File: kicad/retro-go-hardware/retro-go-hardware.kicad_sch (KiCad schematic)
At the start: 1 part

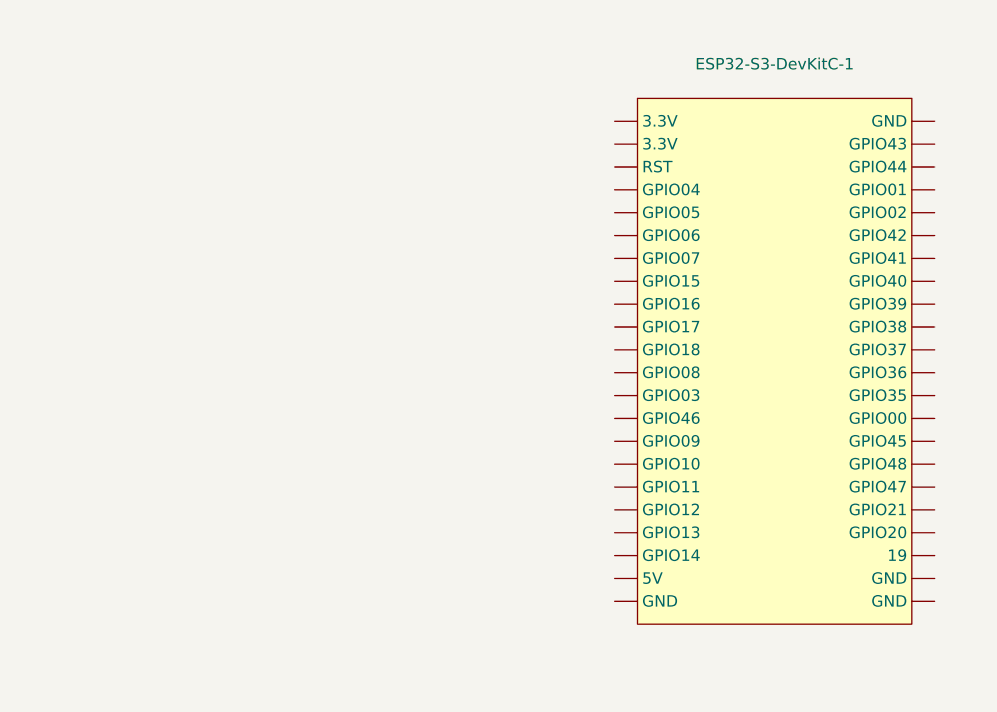
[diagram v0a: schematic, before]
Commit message: Created screen symbol
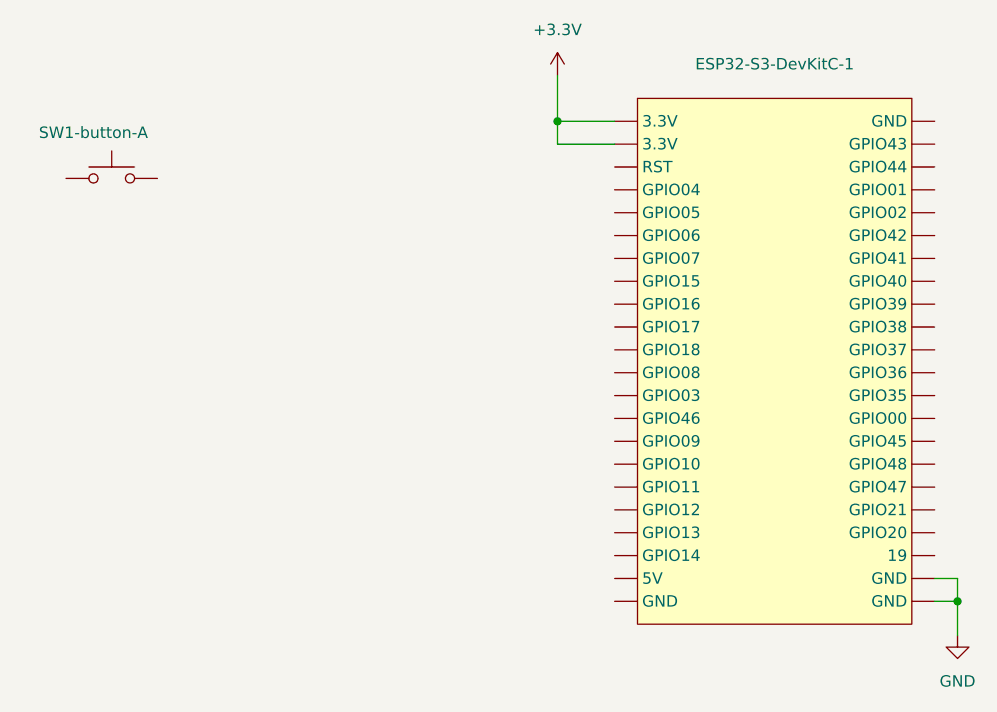
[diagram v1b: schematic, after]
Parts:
- added SW1-button-A: ~, symbol Switch:SW_Push
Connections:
- net GND: now reaches ESP32-S3-DevKitC-1. (RST)
- new net +3.3V: ESP32-S3-DevKitC-1. (RST)

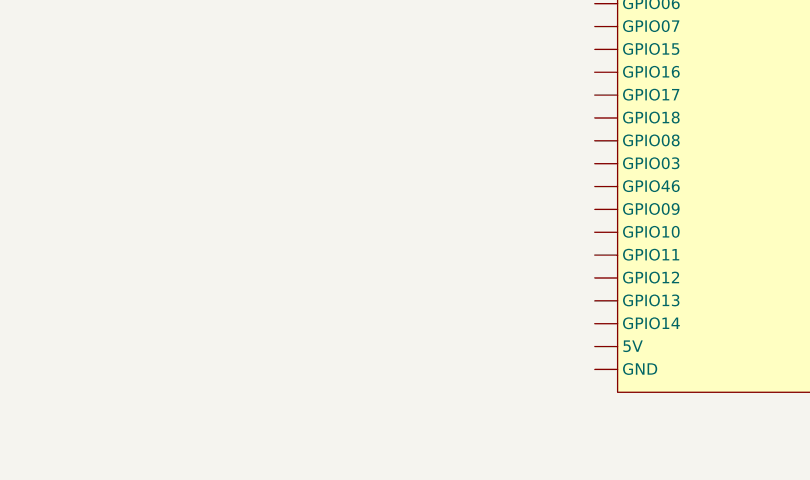
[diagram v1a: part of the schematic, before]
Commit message: Schematics connected SDSPI
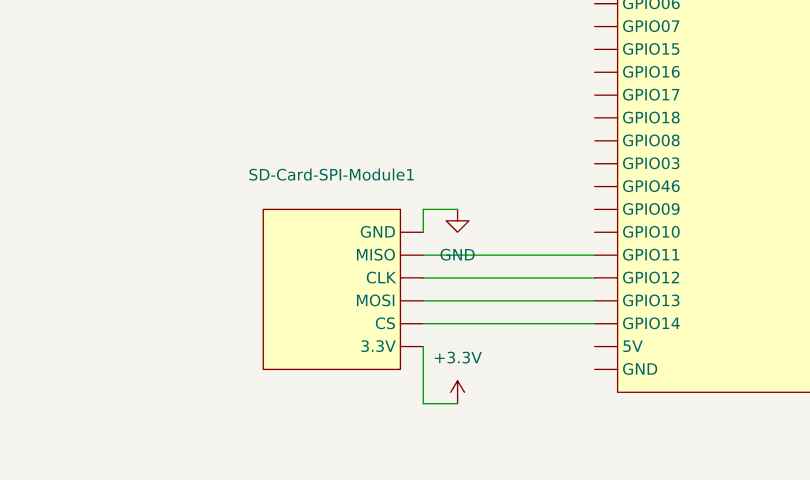
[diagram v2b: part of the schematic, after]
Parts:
- added SD-Card-SPI-Module1: ~, symbol CustomLibrary:SD-Card-SPI-Module
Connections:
- net +3.3V: now also SD-Card-SPI-Module1. (MOSI)
- net GND: now also SD-Card-SPI-Module1. (MOSI)
- new net: ESP32-S3-DevKitC-1. (RST), SD-Card-SPI-Module1. (MOSI) (x4)

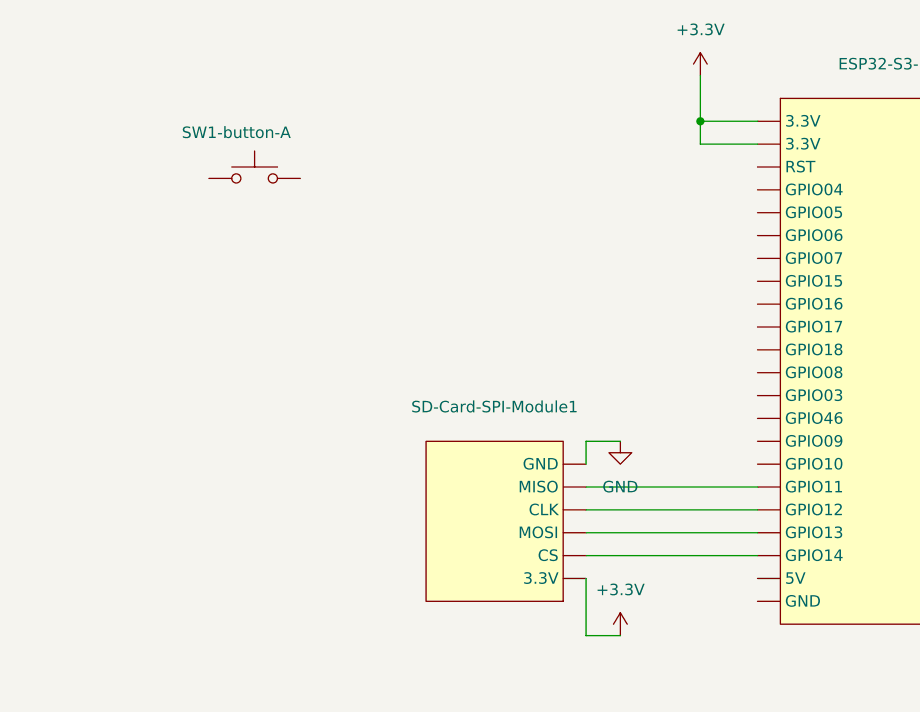
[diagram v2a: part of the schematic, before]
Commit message: Added I2S module to schematic
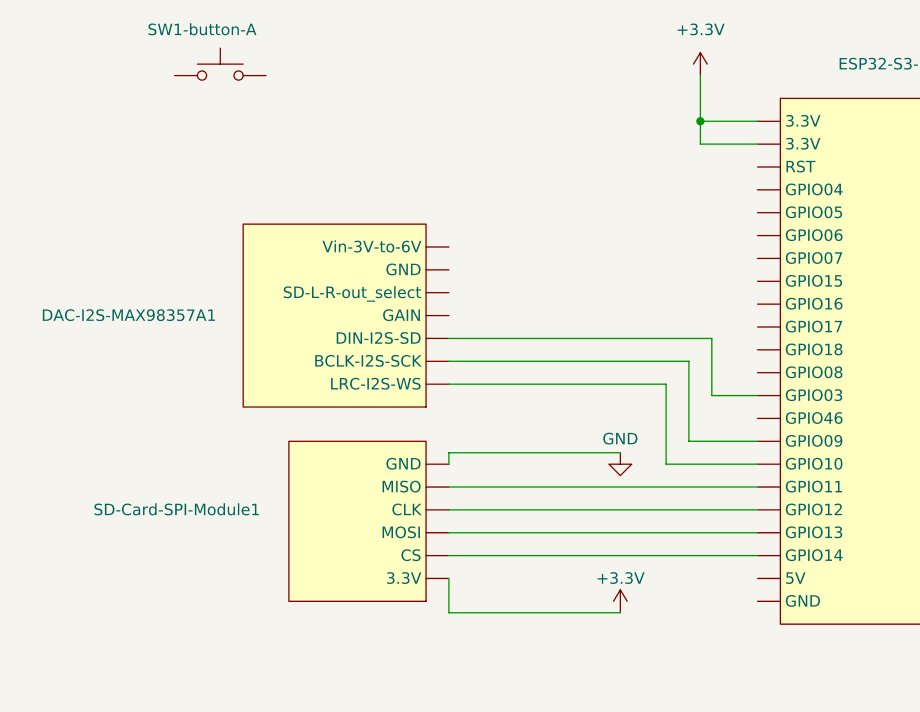
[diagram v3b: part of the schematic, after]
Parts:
- added DAC-I2S-MAX98357A1: ~, symbol CustomLibrary:DAC-I2S-MAX98357A
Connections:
- new net: ESP32-S3-DevKitC-1. (RST), SD-Card-SPI-Module1. (MOSI) (x4)
- new net: DAC-I2S-MAX98357A1. (Vin-3V-to-6V), ESP32-S3-DevKitC-1. (RST) (x3)
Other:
- moved on the sheet: SD-Card-SPI-Module1, SW1-button-A
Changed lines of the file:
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@@
 	(wire
 		(pts
-			(xy 123.19 81.28) (xy 123.19 83.82)
-		)
-		(stroke
-			(width 0)
-			(type default)
-		)
-	)
-	(wire
-		(pts
-			(xy 123.19 96.52) (xy 123.19 102.87)
+			(xy 134.62 72.39) (xy 107.95 72.39)
+		)
+		(stroke
+			(width 0)
+			(type default)
+		)
+	)
+	(wire
+		(pts
+			(xy 107.95 82.55) (xy 107.95 83.82)
+		)
+		(stroke
+			(width 0)
+			(type default)
+		)
+	)
+	(wire
+		(pts
+			(xy 107.95 96.52) (xy 107.95 100.33)
+		)
+		(stroke
+			(width 0)
+			(type default)
+		)
+	)
+	(wire
+		(pts
+			(xy 132.08 74.93) (xy 107.95 74.93)
+		)
+		(stroke
+			(width 0)
+			(type default)
+		)
+	)
+	(wire
+		(pts
+			(xy 132.08 83.82) (xy 132.08 74.93)
 		)
 		(stroke
@@
 	(wire
 		(pts
-			(xy 123.19 88.9) (xy 142.24 88.9)
+			(xy 107.95 88.9) (xy 142.24 88.9)
 		)
 		(stroke
@@
 	(wire
 		(pts
-			(xy 127 81.28) (xy 123.19 81.28)
-		)
-		(stroke
-			(width 0)
-			(type default)
-		)
-	)
-	(wire
-		(pts
-			(xy 123.19 86.36) (xy 142.24 86.36)
+			(xy 137.16 76.2) (xy 137.16 69.85)
+		)
+		(stroke
+			(width 0)
+			(type default)
+		)
+	)
+	(wire
+		(pts
+			(xy 107.95 82.55) (xy 127 82.55)
+		)
+		(stroke
+			(width 0)
+			(type default)
+		)
+	)
+	(wire
+		(pts
+			(xy 107.95 86.36) (xy 142.24 86.36)
 		)
 		(stroke
@@
 	(wire
 		(pts
+			(xy 142.24 76.2) (xy 137.16 76.2)
+		)
+		(stroke
+			(width 0)
+			(type default)
+		)
+	)
+	(wire
+		(pts
 			(xy 142.24 48.26) (xy 135.89 48.26)
 		)
@@
 	(wire
 		(pts
+			(xy 134.62 81.28) (xy 134.62 72.39)
+		)
+		(stroke
+			(width 0)
+			(type default)
+		)
+	)
+	(wire
+		(pts
 			(xy 180.34 96.52) (xy 180.34 99.06)
 		)
@@
 	(wire
 		(pts
+			(xy 142.24 83.82) (xy 132.08 83.82)
+		)
+		(stroke
+			(width 0)
+			(type default)
+		)
+	)
+	(wire
+		(pts
 			(xy 135.89 40.64) (xy 135.89 45.72)
 		)
@@
 	(wire
 		(pts
-			(xy 123.19 102.87) (xy 127 102.87)
+			(xy 107.95 100.33) (xy 127 100.33)
 		)
 		(stroke
@@
 	(wire
 		(pts
-			(xy 123.19 93.98) (xy 142.24 93.98)
+			(xy 107.95 93.98) (xy 142.24 93.98)
 		)
 		(stroke
@@
 	(wire
 		(pts
-			(xy 123.19 91.44) (xy 142.24 91.44)
+			(xy 142.24 81.28) (xy 134.62 81.28)
+		)
+		(stroke
+			(width 0)
+			(type default)
+		)
+	)
+	(wire
+		(pts
+			(xy 137.16 69.85) (xy 107.95 69.85)
+		)
+		(stroke
+			(width 0)
+			(type default)
+		)
+	)
+	(wire
+		(pts
+			(xy 107.95 91.44) (xy 142.24 91.44)
 		)
 		(stroke
@@
 	(symbol
 		(lib_id "power:+3.3V")
-		(at 127 102.87 0)
+		(at 127 100.33 0)
 		(unit 1)
 		(exclude_from_sim no)
@@
 		(on_board yes)
 		(dnp no)
-		(fields_autoplaced yes)
 		(property "Reference" "#PWR04"
-			(at 127 106.68 0)
+			(at 127 104.14 0)
 			(effects
 				(font
@@
 		)
 		(property "Value" "+3.3V"
-			(at 127 97.79 0)
+			(at 127 96.52 0)
 			(effects
 				(font
@@
 		)
 		(property "Footprint" ""
-			(at 127 102.87 0)
+			(at 127 100.33 0)
 			(effects
 				(font
@@
 		)
 		(property "Datasheet" ""
-			(at 127 102.87 0)
+			(at 127 100.33 0)
 			(effects
 				(font
@@
 		)
 		(property "Description" "Power symbol creates a global label with name \"+3.3V\""
-			(at 127 102.87 0)
+			(at 127 100.33 0)
 			(effects
 				(font
@@
 	(symbol
 		(lib_id "Switch:SW_Push")
-		(at 86.36 52.07 0)
+		(at 82.55 40.64 0)
 		(unit 1)
 		(exclude_from_sim no)
@@
 		(dnp no)
 		(property "Reference" "SW1-button-A"
-			(at 84.328 46.99 0)
+			(at 80.518 35.56 0)
 			(effects
 				(font
@@
 		)
 		(property "Value" "~"
-			(at 87.63 46.736 0)
+			(at 83.82 35.306 0)
 			(do_not_autoplace yes)
 			(effects
@@
 		)
 		(property "Footprint" ""
-			(at 86.36 46.99 0)
+			(at 82.55 35.56 0)
 			(effects
 				(font
@@
 		)
 		(property "Datasheet" "~"
-			(at 86.36 46.99 0)
+			(at 82.55 35.56 0)
 			(effects
 				(font
@@
 		)
 		(property "Description" "Push button switch, generic, two pins"
-			(at 86.36 52.07 0)
+			(at 82.55 40.64 0)
 			(effects
 				(font
@@
 	(symbol
 		(lib_id "CustomLibrary:SD-Card-SPI-Module")
-		(at 113.03 88.9 180)
+		(at 97.79 88.9 180)
 		(unit 1)
 		(exclude_from_sim no)
@@
 		(on_board yes)
 		(dnp no)
-		(fields_autoplaced yes)
 		(property "Reference" "SD-Card-SPI-Module1"
-			(at 113.03 77.47 0)
+			(at 77.724 88.9 0)
 			(effects
 				(font
@@
 		)
 		(property "Value" "~"
-			(at 113.03 80.01 0)
+			(at 97.79 80.01 0)
 			(effects
 				(font
@@
 		)
 		(property "Footprint" ""
-			(at 107.95 87.63 90)
+			(at 92.71 87.63 90)
 			(effects
 				(font
@@
 		)
 		(property "Datasheet" ""
-			(at 107.95 87.63 90)
+			(at 92.71 87.63 90)
 			(effects
 				(font
@@
 		)
 		(property "Description" ""
-			(at 107.95 87.63 90)
+			(at 92.71 87.63 90)
 			(effects
 				(font
@@
 	(symbol
 		(lib_id "power:GND")
-		(at 127 81.28 0)
+		(at 127 82.55 0)
 		(unit 1)
 		(exclude_from_sim no)
@@
 		(on_board yes)
 		(dnp no)
-		(fields_autoplaced yes)
 		(property "Reference" "#PWR03"
-			(at 127 87.63 0)
+			(at 127 88.9 0)
 			(effects
 				(font
@@
 		)
 		(property "Value" "GND"
-			(at 127 86.36 0)
+			(at 127 81.026 0)
 			(effects
 				(font
@@
 		)
 		(property "Footprint" ""
-			(at 127 81.28 0)
+			(at 127 82.55 0)
 			(effects
 				(font
@@
 		)
 		(property "Datasheet" ""
-			(at 127 81.28 0)
+			(at 127 82.55 0)
 			(effects
 				(font
@@
 		)
 		(property "Description" "Power symbol creates a global label with name \"GND\" , ground"
-			(at 127 81.28 0)
+			(at 127 82.55 0)
 			(effects
 				(font
@@
 					(unit 1)
 				)
+			)
+		)
+	)
+	(symbol
+		(lib_id "CustomLibrary:DAC-I2S-MAX98357A")
+		(at 95.25 67.31 180)
+		(unit 1)
+		(exclude_from_sim no)
+		(in_bom yes)
+		(on_board yes)
+		(dnp no)
+		(property "Reference" "DAC-I2S-MAX98357A1"
+			(at 72.39 67.31 0)
+			(effects
+				(font
+					(size 1.27 1.27)
+				)
+			)
+		)
+		(property "Value" "~"
+			(at 95.25 55.88 0)
+			(effects
+				(font
+					(size 1.27 1.27)
+				)
+			)
+		)
+		(property "Footprint" ""
+			(at 95.25 67.31 0)
+			(effects
+				(font
+					(size 1.27 1.27)
+				)
+				(hide yes)
+			)
+		)
+		(property "Datasheet" ""
+			(at 95.25 67.31 0)
+			(effects
+				(font
+					(size 1.27 1.27)
+				)
+				(hide yes)
+			)
+		)
+		(property "Description" ""
+			(at 95.25 67.31 0)
+			(effects
+				(font
+					(size 1.27 1.27)
+				)
+				(hide yes)
+			)
+		)
+		(pin ""
+		)
+		(pin ""
+		)
+		(pin ""
+		)
+		(pin ""
+		)
+		(pin ""
+		)
+		(pin ""
+		)
+		(pin ""
+		)
+		(instances
+			(project "retro-go-hardware"
+				(path "/c7a77f24-7c25-4509-9d7f-e0356b19303a"
+					(reference "DAC-I2S-MAX98357A1")
+					(unit 1)
+				)

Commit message: Power supply managed
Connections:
- net GND: now also DAC-I2S-MAX98357A1. (Vin-3V-to-6V)
- new net: ESP32-S3-DevKitC-1. (RST), SD-Card-SPI-Module1. (MOSI) (x4)
- new net: DAC-I2S-MAX98357A1. (Vin-3V-to-6V), ESP32-S3-DevKitC-1. (RST) (x3)
- new net +5V: DAC-I2S-MAX98357A1. (Vin-3V-to-6V), ESP32-S3-DevKitC-1. (RST)

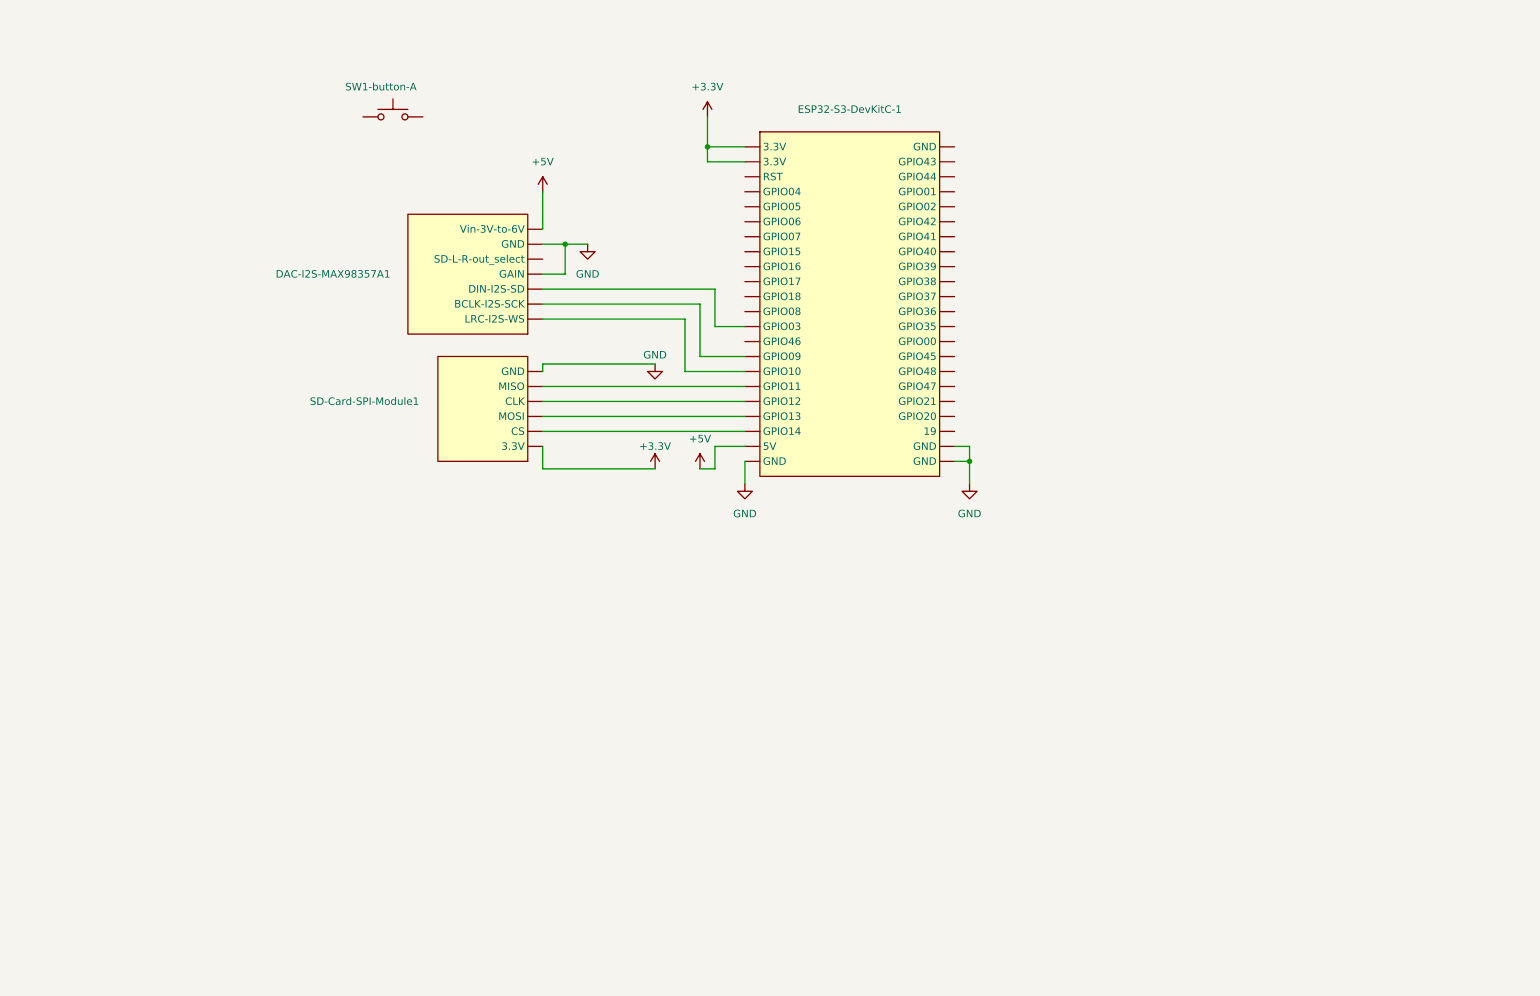
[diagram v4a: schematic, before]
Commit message: Power supply zone
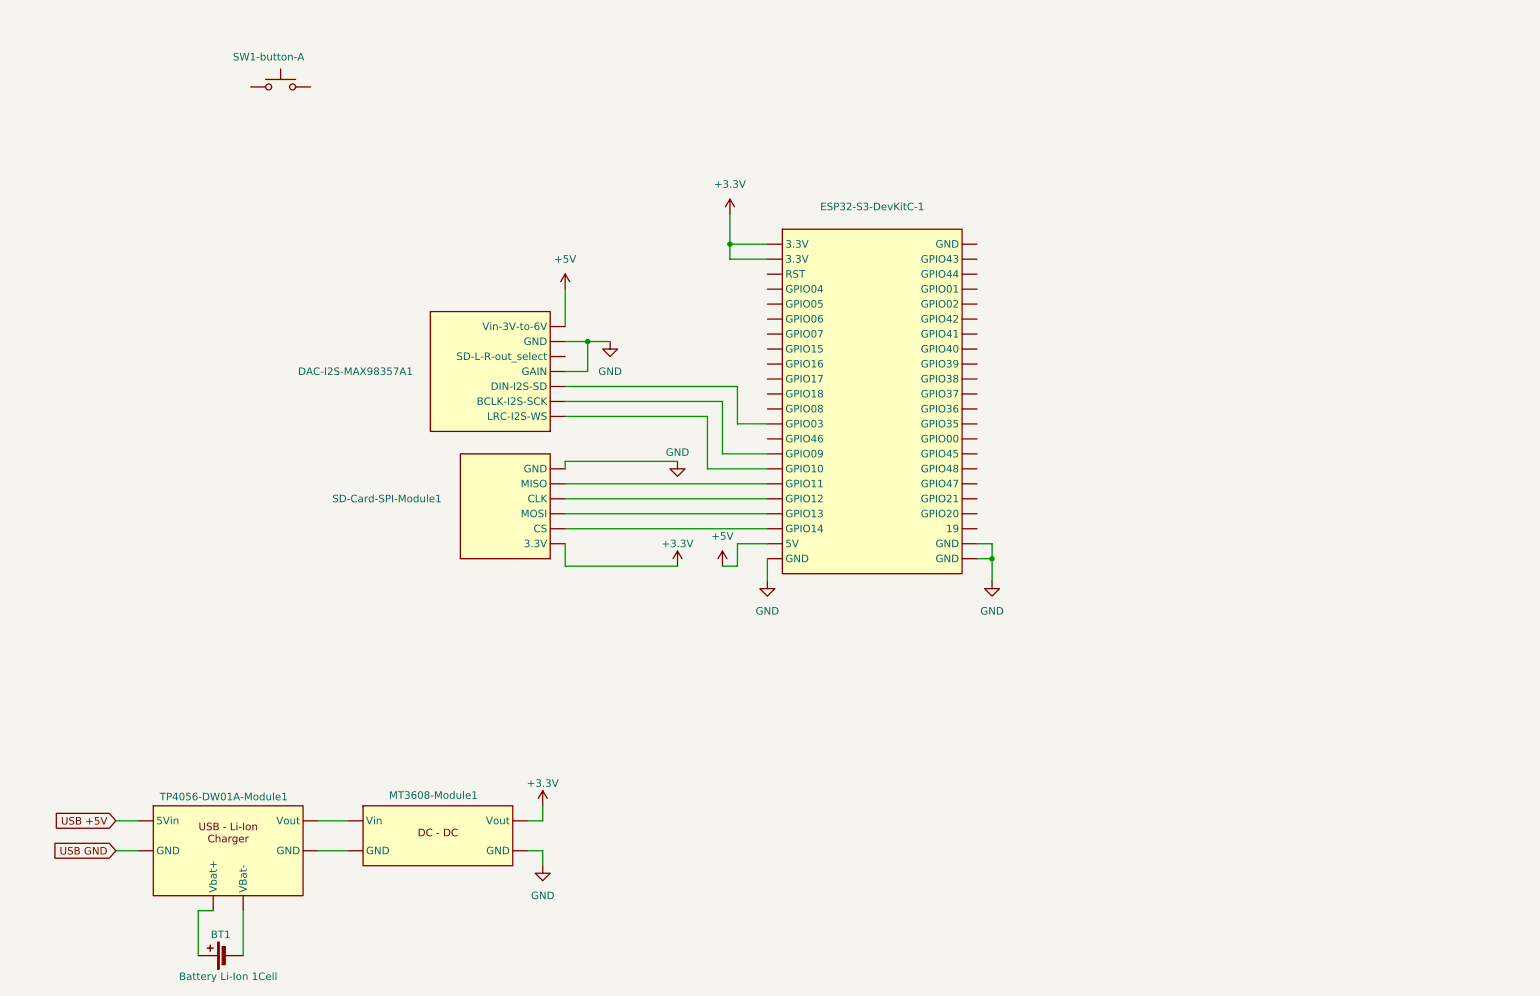
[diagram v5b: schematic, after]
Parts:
- added BT1: Battery Li-Ion 1Cell, symbol Device:Battery_Cell
- added MT3608-Module1: ~, symbol CustomLibrary:MT3608-Module
- added TP4056-DW01A-Module1: ~, symbol CustomLibrary:TP4056-DW01A-Module
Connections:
- net +3.3V: now also MT3608-Module1. (Vout)
- net GND: now also MT3608-Module1. (Vout)
- new net: ESP32-S3-DevKitC-1. (RST), SD-Card-SPI-Module1. (MOSI) (x4)
- new net: BT1.1 (+), TP4056-DW01A-Module1. (Vout)
- new net: BT1.2 (-), TP4056-DW01A-Module1. (Vout)
- new net: DAC-I2S-MAX98357A1. (Vin-3V-to-6V), ESP32-S3-DevKitC-1. (RST) (x3)
- new net: MT3608-Module1. (Vout), TP4056-DW01A-Module1. (Vout) (x2)
- new net USB +5V: TP4056-DW01A-Module1. (Vout)
- new net USB GND: TP4056-DW01A-Module1. (Vout)
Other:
- moved on the sheet: DAC-I2S-MAX98357A1, ESP32-S3-DevKitC-1, SD-Card-SPI-Module1, SW1-button-A
